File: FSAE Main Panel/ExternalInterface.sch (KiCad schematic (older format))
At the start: 0 parts

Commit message: Added CAN components
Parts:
- added J?: Conn_01x04, symbol Conn_01x04
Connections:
- new net CAN_H: J?.2 (Pin_2)
- new net CAN_L: J?.3 (Pin_3)
- new net CAN_V+: J?.1 (Pin_1)
- new net GND: J?.4 (Pin_4)
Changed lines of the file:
@@
 $Descr A4 11693 8268
 encoding utf-8
-Sheet 2 3
+Sheet 2 4
 Title ""
 Date ""
@@
 Comment4 ""
 $EndDescr
+$Comp
+L Conn_01x04 J?
+U 1 1 5BE242F9
+P 4700 3250
+F 0 "J?" H 4700 3450 50  0000 C CNN
+F 1 "Conn_01x04" H 4700 2950 50  0000 C CNN
+F 2 "" H 4700 3250 50  0001 C CNN
+F 3 "" H 4700 3250 50  0001 C CNN
+	1    4700 3250
+	-1   0    0    -1
+$EndComp
+Text Label 4900 3150 0    39   ~ 0
+CAN_V+
+Text Label 4900 3250 0    39   ~ 0
+CAN_H
+Text Label 4900 3350 0    39   ~ 0
+CAN_L
+Text Label 4900 3450 0    39   ~ 0
+GND
+Text GLabel 5550 3150 2    39   Input ~ 0
+CAN_V+
+Wire Wire Line
+	4900 3150 5550 3150
+$Comp
+L GND #PWR?
+U 1 1 5BE24FFA
+P 5200 3650
+F 0 "#PWR?" H 5200 3400 50  0001 C CNN
+F 1 "GND" H 5200 3500 50  0000 C CNN
+F 2 "" H 5200 3650 50  0001 C CNN
+F 3 "" H 5200 3650 50  0001 C CNN
+	1    5200 3650
+	1    0    0    -1
+$EndComp
+Wire Wire Line
+	4900 3450 5200 3450
+Wire Wire Line
+	5200 3450 5200 3650
 $EndSCHEMATC

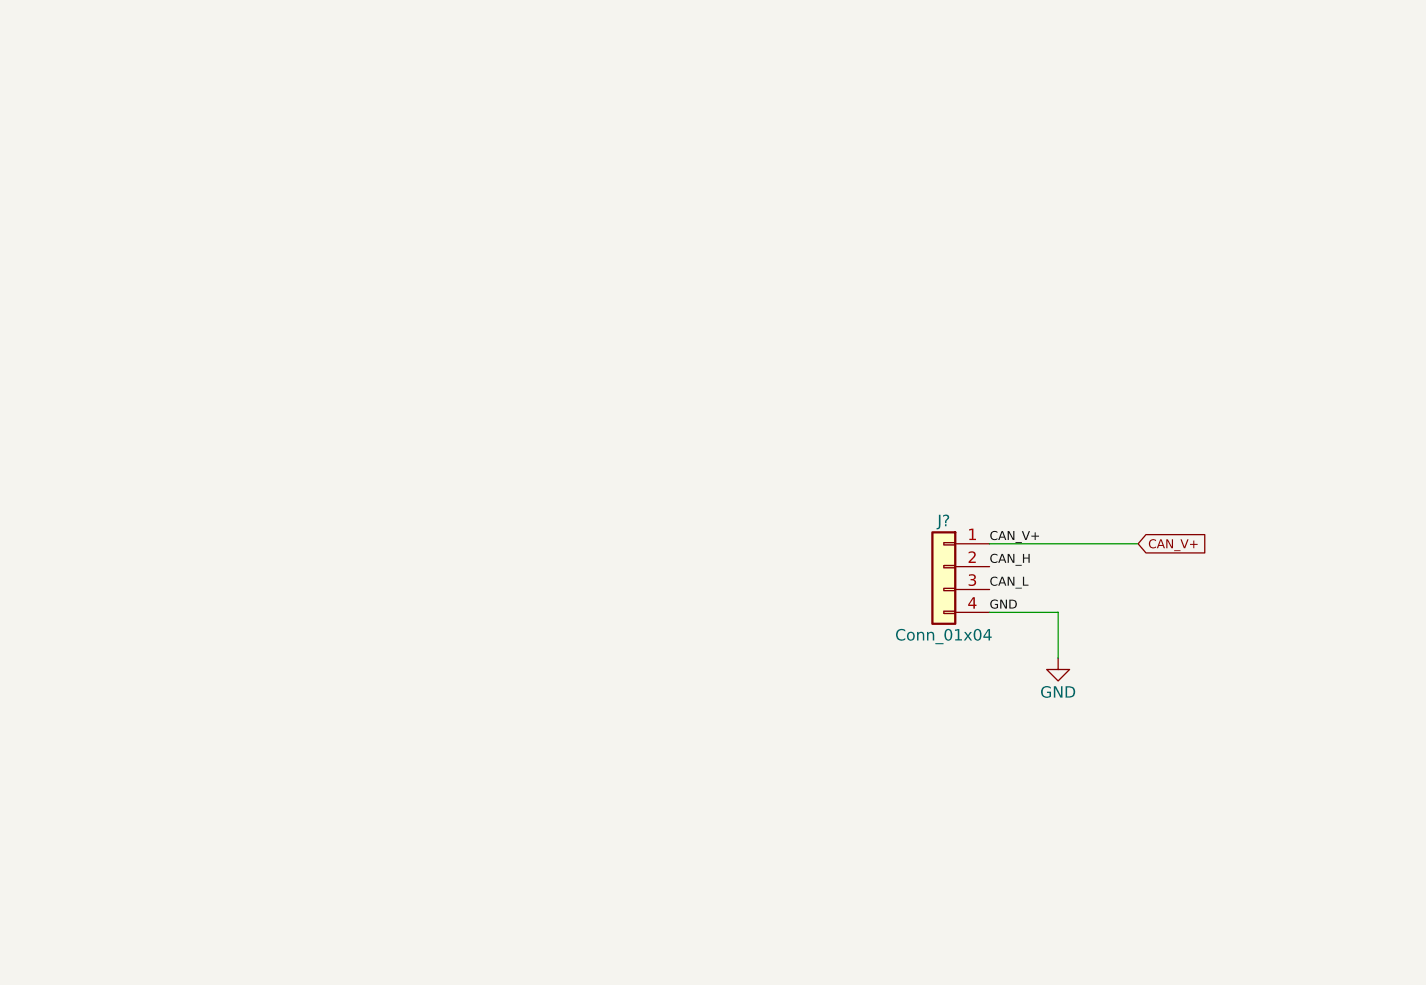
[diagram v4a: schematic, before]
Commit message: Added RPM LED Control
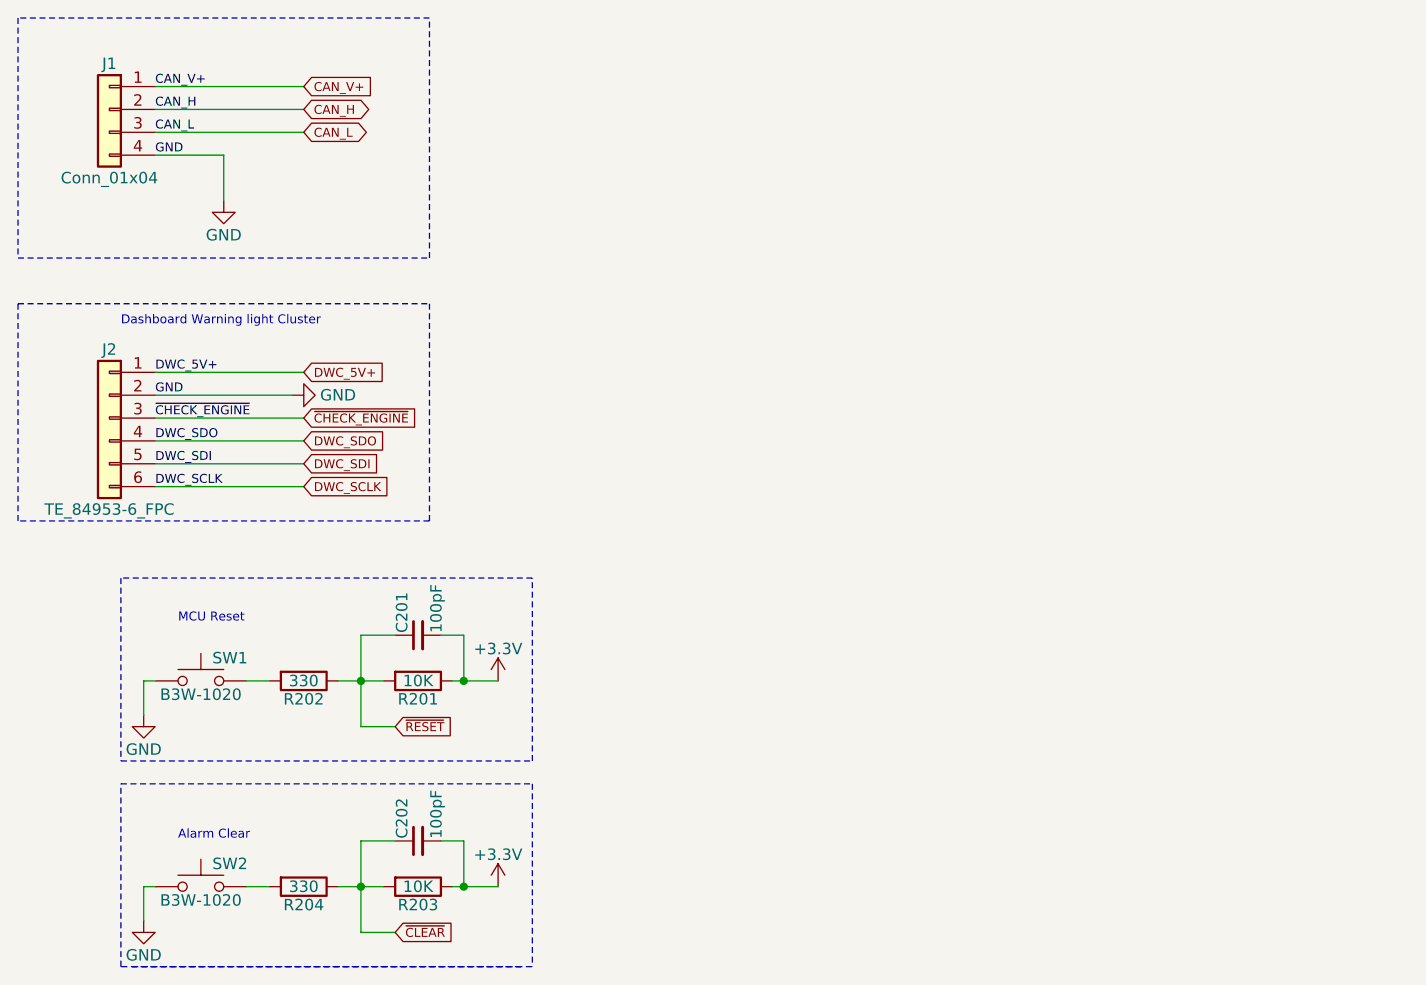
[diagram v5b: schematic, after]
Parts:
- added C201, C202: 100pF, symbol C_Small
- added J2: TE_84953-6_FPC, Connectors_TE-Connectivity:TE_84953-6_1x06_P1.0mm_Horizontal, symbol Conn_01x06
- added R201, R203: 10K, symbol R
- added R202, R204: 330, symbol R
- added SW1, SW2: B3W-1020, Buttons_Switches_THT:SW_TH_Tactile_Omron_B3F-10xx, symbol SW_Push
- gave numbers to parts that had none: 1
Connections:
- net GND: now also J2.2 (Pin_2), SW1.1, SW2.1
- new net: R202.2, SW1.2
- new net: R204.2, SW2.2
- new net +3V3: C201.2, C202.2, R201.1, R203.1
- new net DWC_5V+: J2.1 (Pin_1)
- new net DWC_SCLK: J2.6 (Pin_6)
- new net DWC_SDI: J2.5 (Pin_5)
- new net DWC_SDO: J2.4 (Pin_4)
- new net ~CHECK_ENGINE: J2.3 (Pin_3)
- new net ~CLEAR: C202.1, R203.2, R204.1
- new net ~RESET: C201.1, R201.2, R202.1
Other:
- note added: "Alarm Clear"
- note added: "Dashboard Warning light Cluster"
- note added: "MCU Reset"
- moved on the sheet: J1

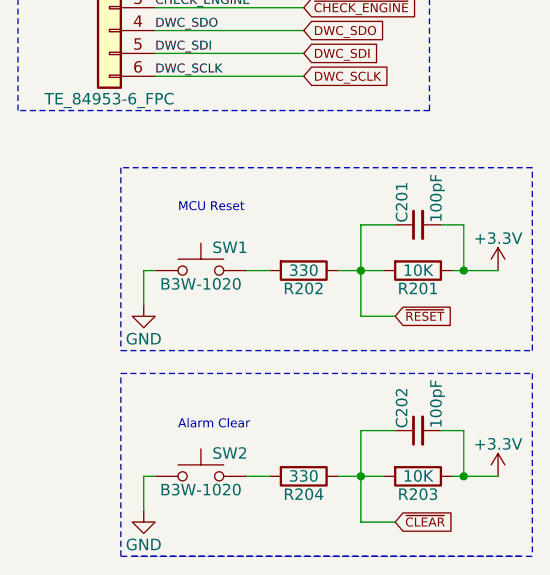
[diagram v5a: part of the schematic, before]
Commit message: Finished most LEDs, begun power regulators
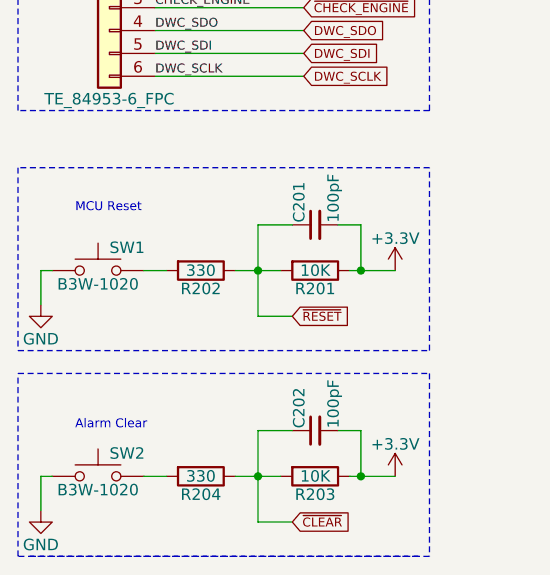
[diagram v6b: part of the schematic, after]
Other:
- moved on the sheet: C201, C202, R201, R202, R203, R204, SW1, SW2
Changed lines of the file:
@@
 L SW_Push SW1
 U 1 1 5BE9B978
-P 1450 3750
-F 0 "SW1" H 1500 3850 50  0000 L CNN
-F 1 "B3W-1020" H 1450 3690 50  0000 C CNN
-F 2 "Buttons_Switches_THT:SW_TH_Tactile_Omron_B3F-10xx" H 1450 3950 50  0001 C CNN
-F 3 "https://www.mouser.com/datasheet/2/307/en-b3w-779787.pdf" H 1450 3950 50  0001 C CNN
-F 4 "Omron" H 1450 3750 60  0001 C CNN "Manufacturer"
-	1    1450 3750
-	1    0    0    -1
-$EndComp
-Text Notes 1350 3500 0    39   ~ 0
+P 1000 3750
+F 0 "SW1" H 1050 3850 50  0000 L CNN
+F 1 "B3W-1020" H 1000 3690 50  0000 C CNN
+F 2 "Buttons_Switches_THT:SW_TH_Tactile_Omron_B3F-10xx" H 1000 3950 50  0001 C CNN
+F 3 "https://www.mouser.com/datasheet/2/307/en-b3w-779787.pdf" H 1000 3950 50  0001 C CNN
+F 4 "Omron" H 1000 3750 60  0001 C CNN "Manufacturer"
+	1    1000 3750
+	1    0    0    -1
+$EndComp
+Text Notes 900  3500 0    39   ~ 0
 MCU Reset
 $Comp
 L SW_Push SW2
 U 1 1 5BE9BA9C
-P 1450 4650
-F 0 "SW2" H 1500 4750 50  0000 L CNN
-F 1 "B3W-1020" H 1450 4590 50  0000 C CNN
-F 2 "Buttons_Switches_THT:SW_TH_Tactile_Omron_B3F-10xx" H 1450 4850 50  0001 C CNN
-F 3 "https://www.mouser.com/datasheet/2/307/en-b3w-779787.pdf" H 1450 4850 50  0001 C CNN
-F 4 "Omron" H 1450 4650 60  0001 C CNN "Manufacturer"
-	1    1450 4650
-	1    0    0    -1
-$EndComp
-Text Notes 1350 4450 0    39   ~ 0
+P 1000 4650
+F 0 "SW2" H 1050 4750 50  0000 L CNN
+F 1 "B3W-1020" H 1000 4590 50  0000 C CNN
+F 2 "Buttons_Switches_THT:SW_TH_Tactile_Omron_B3F-10xx" H 1000 4850 50  0001 C CNN
+F 3 "https://www.mouser.com/datasheet/2/307/en-b3w-779787.pdf" H 1000 4850 50  0001 C CNN
+F 4 "Omron" H 1000 4650 60  0001 C CNN "Manufacturer"
+	1    1000 4650
+	1    0    0    -1
+$EndComp
+Text Notes 900  4450 0    39   ~ 0
 Alarm Clear
 $Comp
 L GND #PWR?
 U 1 1 5BE9BAFE
-P 1200 3900
-F 0 "#PWR?" H 1200 3650 50  0001 C CNN
-F 1 "GND" H 1200 3750 50  0000 C CNN
-F 2 "" H 1200 3900 50  0001 C CNN
-F 3 "" H 1200 3900 50  0001 C CNN
-	1    1200 3900
+P 750 3900
+F 0 "#PWR?" H 750 3650 50  0001 C CNN
+F 1 "GND" H 750 3750 50  0000 C CNN
+F 2 "" H 750 3900 50  0001 C CNN
+F 3 "" H 750 3900 50  0001 C CNN
+	1    750  3900
 	1    0    0    -1
 $EndComp
@@
 L GND #PWR?
 U 1 1 5BE9BB22
-P 1200 4800
-F 0 "#PWR?" H 1200 4550 50  0001 C CNN
-F 1 "GND" H 1200 4650 50  0000 C CNN
-F 2 "" H 1200 4800 50  0001 C CNN
-F 3 "" H 1200 4800 50  0001 C CNN
-	1    1200 4800
-	1    0    0    -1
-$EndComp
-Wire Wire Line
-	1250 4650 1200 4650
-Wire Wire Line
-	1200 4650 1200 4800
-Wire Wire Line
-	1250 3750 1200 3750
-Wire Wire Line
-	1200 3750 1200 3900
+P 750 4800
+F 0 "#PWR?" H 750 4550 50  0001 C CNN
+F 1 "GND" H 750 4650 50  0000 C CNN
+F 2 "" H 750 4800 50  0001 C CNN
+F 3 "" H 750 4800 50  0001 C CNN
+	1    750  4800
+	1    0    0    -1
+$EndComp
+Wire Wire Line
+	800  4650 750  4650
+Wire Wire Line
+	750  4650 750  4800
+Wire Wire Line
+	800  3750 750  3750
+Wire Wire Line
+	750  3750 750  3900
 $Comp
 L R R201
 U 1 1 5BE9BDD1
-P 2400 3750
-F 0 "R201" V 2480 3750 50  0000 C CNN
-F 1 "10K" V 2400 3750 50  0000 C CNN
-F 2 "" V 2330 3750 50  0001 C CNN
-F 3 "" H 2400 3750 50  0001 C CNN
-	1    2400 3750
-	0    1    1    0
-$EndComp
-Wire Wire Line
-	2050 3750 2150 3750
-Wire Wire Line
-	2150 3750 2250 3750
-Wire Wire Line
-	2750 3750 2600 3750
-Wire Wire Line
-	2600 3750 2550 3750
-Wire Wire Line
-	2150 3550 2150 3750
-Wire Wire Line
-	2150 3750 2150 3950
-Connection ~ 2150 3750
-Text GLabel 2300 3950 2    39   Input ~ 0
+P 1950 3750
+F 0 "R201" V 2030 3750 50  0000 C CNN
+F 1 "10K" V 1950 3750 50  0000 C CNN
+F 2 "" V 1880 3750 50  0001 C CNN
+F 3 "" H 1950 3750 50  0001 C CNN
+	1    1950 3750
+	0    1    1    0
+$EndComp
+Wire Wire Line
+	1600 3750 1800 3750
+Wire Wire Line
+	2100 3750 2300 3750
+Wire Wire Line
+	1700 3550 1700 3950
+Connection ~ 1700 3750
+Text GLabel 1850 3950 2    39   Input ~ 0
 ~RESET
 Wire Notes Line
-	1100 4200 2900 4200
-Wire Notes Line
-	2900 4200 2900 5000
-Wire Notes Line
-	2850 5000 1100 5000
-Wire Notes Line
-	1100 5000 1100 4200
-Wire Notes Line
-	1100 4100 2900 4100
-Wire Notes Line
-	2900 4100 2900 3300
-Wire Notes Line
-	2900 3300 1100 3300
-Wire Notes Line
-	1100 3300 1100 4100
+	650  4200 2450 4200
+Wire Notes Line
+	2450 4200 2450 5000
+Wire Notes Line
+	2400 5000 650  5000
+Wire Notes Line
+	650  5000 650  4200
+Wire Notes Line
+	650  4100 2450 4100
+Wire Notes Line
+	2450 4100 2450 3300
+Wire Notes Line
+	2450 3300 650  3300
+Wire Notes Line
+	650  3300 650  4100
 Wire Notes Line
 	650  1900 2450 1900
@@
 L C_Small C201
 U 1 1 5BE9C881
-P 2400 3550
-F 0 "C201" H 2410 3620 50  0000 L CNN
-F 1 "100pF" H 2410 3470 50  0000 L CNN
-F 2 "" H 2400 3550 50  0001 C CNN
-F 3 "" H 2400 3550 50  0001 C CNN
-	1    2400 3550
+P 1950 3550
+F 0 "C201" H 1960 3620 50  0000 L CNN
+F 1 "100pF" H 1960 3470 50  0000 L CNN
+F 2 "" H 1950 3550 50  0001 C CNN
+F 3 "" H 1950 3550 50  0001 C CNN
+	1    1950 3550
 	0    -1   -1   0
 $EndComp
@@
 L R R202
 U 1 1 5BE9C8E2
-P 1900 3750
-F 0 "R202" V 1980 3750 50  0000 C CNN
-F 1 "330" V 1900 3750 50  0000 C CNN
-F 2 "" V 1830 3750 50  0001 C CNN
-F 3 "" H 1900 3750 50  0001 C CNN
-	1    1900 3750
-	0    1    1    0
-$EndComp
-Wire Wire Line
-	1650 3750 1750 3750
-Wire Wire Line
-	2150 3950 2300 3950
-Wire Wire Line
-	2150 3550 2300 3550
-Wire Wire Line
-	2500 3550 2600 3550
-Wire Wire Line
-	2600 3550 2600 3750
-Connection ~ 2600 3750
+P 1450 3750
+F 0 "R202" V 1530 3750 50  0000 C CNN
+F 1 "330" V 1450 3750 50  0000 C CNN
+F 2 "" V 1380 3750 50  0001 C CNN
+F 3 "" H 1450 3750 50  0001 C CNN
+	1    1450 3750
+	0    1    1    0
+$EndComp
+Wire Wire Line
+	1200 3750 1300 3750
+Wire Wire Line
+	1700 3950 1850 3950
+Wire Wire Line
+	1700 3550 1850 3550
+Wire Wire Line
+	2050 3550 2150 3550
+Wire Wire Line
+	2150 3550 2150 3750
+Connection ~ 2150 3750
 $Comp
 L R R203
 U 1 1 5BE9CBCA
-P 2400 4650
-F 0 "R203" V 2480 4650 50  0000 C CNN
-F 1 "10K" V 2400 4650 50  0000 C CNN
-F 2 "" V 2330 4650 50  0001 C CNN
-F 3 "" H 2400 4650 50  0001 C CNN
-	1    2400 4650
-	0    1    1    0
-$EndComp
-Wire Wire Line
-	2050 4650 2150 4650
-Wire Wire Line
-	2150 4650 2250 4650
-Wire Wire Line
-	2750 4650 2600 4650
-Wire Wire Line
-	2600 4650 2550 4650
-Wire Wire Line
-	2150 4450 2150 4650
-Wire Wire Line
-	2150 4650 2150 4850
-Connection ~ 2150 4650
-Text GLabel 2300 4850 2    39   Input ~ 0
+P 1950 4650
+F 0 "R203" V 2030 4650 50  0000 C CNN
+F 1 "10K" V 1950 4650 50  0000 C CNN
+F 2 "" V 1880 4650 50  0001 C CNN
+F 3 "" H 1950 4650 50  0001 C CNN
+	1    1950 4650
+	0    1    1    0
+$EndComp
+Wire Wire Line
+	1600 4650 1800 4650
+Wire Wire Line
+	2100 4650 2300 4650
+Wire Wire Line
+	1700 4450 1700 4850
+Connection ~ 1700 4650
+Text GLabel 1850 4850 2    39   Input ~ 0
 ~CLEAR
 Wire Notes Line
-	1150 5000 2900 5000
+	2450 5000 700  5000
 $Comp
 L C_Small C202
 U 1 1 5BE9CBDF
-P 2400 4450
-F 0 "C202" H 2410 4520 50  0000 L CNN
-F 1 "100pF" H 2410 4370 50  0000 L CNN
-F 2 "" H 2400 4450 50  0001 C CNN
-F 3 "" H 2400 4450 50  0001 C CNN
-	1    2400 4450
+P 1950 4450
+F 0 "C202" H 1960 4520 50  0000 L CNN
+F 1 "100pF" H 1960 4370 50  0000 L CNN
+F 2 "" H 1950 4450 50  0001 C CNN
+F 3 "" H 1950 4450 50  0001 C CNN
+	1    1950 4450
 	0    -1   -1   0
 $EndComp
@@
 L R R204
 U 1 1 5BE9CBE5
-P 1900 4650
-F 0 "R204" V 1980 4650 50  0000 C CNN
-F 1 "330" V 1900 4650 50  0000 C CNN
-F 2 "" V 1830 4650 50  0001 C CNN
-F 3 "" H 1900 4650 50  0001 C CNN
-	1    1900 4650
-	0    1    1    0
-$EndComp
-Wire Wire Line
-	1650 4650 1750 4650
-Wire Wire Line
-	2150 4850 2300 4850
-Wire Wire Line
-	2150 4450 2300 4450
-Wire Wire Line
-	2500 4450 2600 4450
-Wire Wire Line
-	2600 4450 2600 4650
-Connection ~ 2600 4650
+P 1450 4650
+F 0 "R204" V 1530 4650 50  0000 C CNN
+F 1 "330" V 1450 4650 50  0000 C CNN
+F 2 "" V 1380 4650 50  0001 C CNN
+F 3 "" H 1450 4650 50  0001 C CNN
+	1    1450 4650
+	0    1    1    0
+$EndComp
+Wire Wire Line
+	1200 4650 1300 4650
+Wire Wire Line
+	1700 4850 1850 4850
+Wire Wire Line
+	1700 4450 1850 4450
+Wire Wire Line
+	2050 4450 2150 4450
+Wire Wire Line
+	2150 4450 2150 4650
+Connection ~ 2150 4650
 $Comp
 L +3.3V #PWR?
 U 1 1 5BE9CCF2
-P 2750 3750
-F 0 "#PWR?" H 2750 3600 50  0001 C CNN
-F 1 "+3.3V" H 2750 3890 50  0000 C CNN
-F 2 "" H 2750 3750 50  0001 C CNN
-F 3 "" H 2750 3750 50  0001 C CNN
-	1    2750 3750
+P 2300 3750
+F 0 "#PWR?" H 2300 3600 50  0001 C CNN
+F 1 "+3.3V" H 2300 3890 50  0000 C CNN
+F 2 "" H 2300 3750 50  0001 C CNN
+F 3 "" H 2300 3750 50  0001 C CNN
+	1    2300 3750
 	1    0    0    -1
 $EndComp
@@
 L +3.3V #PWR?
 U 1 1 5BE9CD22
-P 2750 4650
-F 0 "#PWR?" H 2750 4500 50  0001 C CNN
-F 1 "+3.3V" H 2750 4790 50  0000 C CNN
-F 2 "" H 2750 4650 50  0001 C CNN
-F 3 "" H 2750 4650 50  0001 C CNN
-	1    2750 4650
-	1    0    0    -1
-$EndComp
+P 2300 4650
+F 0 "#PWR?" H 2300 4500 50  0001 C CNN
+F 1 "+3.3V" H 2300 4790 50  0000 C CNN
+F 2 "" H 2300 4650 50  0001 C CNN
+F 3 "" H 2300 4650 50  0001 C CNN
+	1    2300 4650
+	1    0    0    -1
+$EndComp
